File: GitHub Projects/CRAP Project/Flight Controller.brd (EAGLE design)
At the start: 40 x 75 mm, 47 parts

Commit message: Changed Module Offsets
Changed module offsets to different values so that the giant names would
go away.  I feel that in future versions this feature will be more
refined, since in V7.7 was the very first version it appeared in.  The
manual inside of the Eagle install in C:/ thankfully is updated with the
new features and explains some of the new ways to do things better than
anywhere I can find online.  Seems that nobody online has these issues,
or I suppose that they just automatically think to read the 1000 page
document every update.
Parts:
- renumbered DCDC_REGULATOR1:C1 to C101, DCDC_REGULATOR1:C10 to C110, DCDC_REGULATOR1:C11 to C111, DCDC_REGULATOR1:C2 to C102, DCDC_REGULATOR1:C3 to C103, DCDC_REGULATOR1:C4 to C104, DCDC_REGULATOR1:C5 to C105, DCDC_REGULATOR1:C6 to C106, DCDC_REGULATOR1:C7 to C107, DCDC_REGULATOR1:C8 to C108, DCDC_REGULATOR1:C9 to C109, DCDC_REGULATOR1:L1 to L101, DCDC_REGULATOR1:Q1 to Q101, DCDC_REGULATOR1:Q2 to Q102, DCDC_REGULATOR1:R1 to R101, DCDC_REGULATOR1:R2 to R102, DCDC_REGULATOR1:R3 to R103, DCDC_REGULATOR1:R4 to R104, DCDC_REGULATOR1:R5 to R105, DCDC_REGULATOR1:R6 to R106, DCDC_REGULATOR1:U$1 to U$101, M:C1 to C201, M:U1 to U201, ORDNANCE1:C1 to C301, ORDNANCE1:C2 to C302, ORDNANCE1:C3 to C303, ORDNANCE1:C4 to C304, ORDNANCE1:R1 to R301, ORDNANCE1:R2 to R302, ORDNANCE1:R3 to R303, ORDNANCE1:R4 to R304, ORDNANCE1:U1 to U301, RTD1:C1 to C401, RTD1:C2 to C402, RTD1:C3 to C403, RTD1:C4 to C404, RTD1:C5 to C405, RTD1:C6 to C406, RTD1:C7 to C407, RTD1:R2 to R402, RTD1:R4 to R404, RTD1:R5 to R405, RTD1:R6 to R406, RTD1:R7 to R407, RTD1:U$1 to U$401, RTD1:U$2 to U$402
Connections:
- net M:+3V3 renamed MS5611:+3V3
- net M:GND renamed MS5611:GND

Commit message: RTD module nearly done
1. RTD module is nearly done. Just need to figure out the connections in
and out of modules, especially for the serial data lines and power.
2. Touched up power and ordnance modules to include the correct ground
symbols.
Note: All this was done with the Eagle 7.x version files
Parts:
- removed C404, C405, C406, C407: 1u, rcl:C0603
- removed R405, R406, R407: 15k, rcl:R0603
- removed U$402: MAX4377T, maxim:UMAX8
- added J401: 4POS_SCREWTERM, CRAP Parts:4POS_0.1
- added R401, R403: 1.2 k, rcl:R0603
- C401, C402: value 1u -> 0.1 u
- C403: value 1u -> 100 n
- R402: value 15k -> 1.2 k
- R404: value 15k -> 10 M
- U$401: value MCP1501-18 -> MAX31865; device microchip:SOT23-6 -> maxim:TQFN20-5X5
- moved R402 16.5 mm to (-53.0, -187.0)
- moved C401 13.3 mm to (-51.0, -170.0)
- moved R404 11.4 mm to (-53.0, -197.0)
- moved U$401 11.0 mm to (-50.0, -162.0)
- moved C402 8.54 mm to (-51.0, -174.0)
- moved C403 5.00 mm to (-51.0, -178.0)
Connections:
- net DCDC_REGULATOR1:N$6 renamed DCDC_REGULATOR1:3V3_OUT_RTN
- removed net DCDC_REGULATOR1:N$15: C101.2, C102.2, C103.2
- removed net DCDC_REGULATOR1:N$8: U$101.P$10, U$101.P$4
- removed net ORDNANCE1:N$4: C301.2, C303.2
- removed net ORDNANCE1:N$7: R303.1
- removed net ORDNANCE1:N$9: U301.P11, U301.P8
- removed net RTD1:S1+: U$402.3
- removed net RTD1:S1–: U$402.2
- removed net RTD1:S2+: U$402.5
- removed net RTD1:S2–: U$402.6
- new net DCDC_REGULATOR1:GND: C101.2, C102.2, C103.2, C104.2, C105.2, Q101.1, R102.2, U$101.P$10, U$101.P$4
- new net ORDNANCE1:GND: C301.2, C303.2, C304.2, R303.1, U301.P11, U301.P8
- new net RTD1:N$14: U$401.18
- new net RTD1:N$5: R404.1, U$401.2
- new net RTD1:N$6: C403.1, J401.P$3, U$401.7
- net DCDC_REGULATOR1:N$2: no longer Q101.1
- net RTD1:GND: now also C401.2, C402.2, U$401.10, U$401.15, U$401.16, U$401.6, U$401.EXP; no longer U$402.4
- net RTD1:N$1: now also R401.2, R403.2, R404.2; no longer C402.1
- net RTD1:N$10: now also U$401.13; no longer R406.2, U$402.7
- net RTD1:N$11: now also J401.P$4, U$401.5; no longer C406.1, R406.1, R407.2
- net RTD1:N$12: now also U$401.12; no longer C407.1, R407.1
- net RTD1:N$13: now also U$401.11; no longer C405.2, U$402.8
- net RTD1:N$2: now also C402.1, U$401.19; no longer C401.1, U$401.6
- net RTD1:N$3: now also C401.1, U$401.20; no longer U$401.2, U$401.3
- net RTD1:N$4: now also R401.1, R402.1, R403.1, U$401.3, U$401.4; no longer U$401.5
- net RTD1:N$7: now also C403.2, J401.P$2, U$401.8; no longer R404.2, U$402.1
- net RTD1:N$8: now also J401.P$1, U$401.9; no longer C403.1, R404.1, R405.2
- net RTD1:N$9: now also U$401.14; no longer C404.1, R405.1

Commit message: Fixed the board consistency by making a new board
Do not modify the schematic unless the schematic and board are
consistant.  The easiest way to do this is to just have the board open
when you open the schematic.  This is why it asks if you want to open
both when you first open the program.

Also added a fancy logo to the Atmel chip's footprint, also found an
existing part for the Xbee900 Pro, so I added that into the schematic
and made a module for it.

Also added in modules for the memory and GPS.  That will be what I work
on next.

Outstanding things:  I think the power module is a little funky with the
ports you have on there, Cooper. Are the two return lines not a common
ground?  Why separate them?  Also I recommend changing the ports on the
module to reflect any new net name changes, as well as having a
consistent direction of the pin, so set them to "pwr" when you create
them.  This will come in handy later with design rule checks, because
it'll flag any inconsistancies.
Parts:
- added C1: 4.7u, rcl:C0603
- added C2, C502: 1u, rcl:C0603
- added C3: 100n, rcl:C0603
- added C501: 0.1u, rcl:C0603
- added D301: STPS3045C, diode:TO263AB
- added ORDNANCE1:FIRING_CIRCUIT1:R1, ORDNANCE1:FIRING_CIRCUIT1:R2, ORDNANCE1:FIRING_CIRCUIT1:R3, ORDNANCE1:FIRING_CIRCUIT1:R4: 10 k, rcl:R0603
- added ORDNANCE1:FIRING_CIRCUIT1:U$1: PMF170XP, transistor-power:SOT323
- added ORDNANCE1:FIRING_CIRCUIT1:U$2: DMG4800LSD, transistor-power:SO-08
- added U$1: 2POS_SCREWTERM, CRAP Parts:2POS_0.1
- added U1: (no value), atmel:SQFP-S-10X10-64
- added XB501: XBEE-PRO, maxstream:XBEE-PRO
- JP1: device pinhead:2X03 -> atmel:2X05
- moved R404 308.8 mm to (-24.1, 110.5)
- moved R403 304.5 mm to (-17.8, 110.5)
- moved R402 287.9 mm to (-71.1, 100.3)
- moved R401 282.6 mm to (-64.8, 100.3)
- moved C403 278.4 mm to (-45.7, 100.3)
- moved C402 274.4 mm to (-58.4, 100.3)
- moved C401 270.3 mm to (-52.1, 100.3)
- moved U$401 266.5 mm to (-20.3, 102.9)
- moved J401 262.6 mm to (-35.6, 101.6)
- moved C304 218.7 mm to (-24.1, 66.0)
- moved R304 194.8 mm to (-71.1, 45.7)
- moved C303 194.4 mm to (-17.8, 66.0)
- moved C111 192.9 mm to (-41.9, 88.9)
- moved R303 189.0 mm to (-64.8, 45.7)
- moved C110 186.0 mm to (-35.6, 88.9)
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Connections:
- removed net DCDC_REGULATOR1:3V3_OUT: C106.1, C107.1, C108.1, C109.1, C110.1, C111.1, R103.2, R105.2, U$101.P$7, U$101.P$8
- removed net MS5611:+3V3: C201.1, U201.1
- removed net MS5611:GND: C201.2, U201.2, U201.3
- removed net X_PDI_DATA: JP1.6
- removed net X_RESET_PDI_CLK: JP1.2
- new net N$1: JP1.2, U1.54
- new net N$2: JP1.4, U1.55
- new net N$3: JP1.6, U1.50
- new net N$4: JP1.8, U1.62
- new net N$5: JP1.10, U1.2
- new net N$9: U$1.P$2
- new net ORDNANCE1:FIRING_CIRCUIT1:GND: ORDNANCE1:FIRING_CIRCUIT1:R2.1, ORDNANCE1:FIRING_CIRCUIT1:R3.1, ORDNANCE1:FIRING_CIRCUIT1:U$2.3
- new net ORDNANCE1:FIRING_CIRCUIT1:N$1: ORDNANCE1:FIRING_CIRCUIT1:U$2.1, ORDNANCE1:FIRING_CIRCUIT1:U$2.5, ORDNANCE1:FIRING_CIRCUIT1:U$2.6
- new net ORDNANCE1:FIRING_CIRCUIT1:N$2: ORDNANCE1:FIRING_CIRCUIT1:U$2.7, ORDNANCE1:FIRING_CIRCUIT1:U$2.8
- new net ORDNANCE1:FIRING_CIRCUIT1:N$3: ORDNANCE1:FIRING_CIRCUIT1:R1.1
- new net ORDNANCE1:FIRING_CIRCUIT1:N$4: ORDNANCE1:FIRING_CIRCUIT1:R3.2, ORDNANCE1:FIRING_CIRCUIT1:U$2.2
- new net ORDNANCE1:FIRING_CIRCUIT1:N$5: ORDNANCE1:FIRING_CIRCUIT1:R2.2, ORDNANCE1:FIRING_CIRCUIT1:U$2.4
- new net ORDNANCE1:FIRING_CIRCUIT1:N$6: ORDNANCE1:FIRING_CIRCUIT1:R1.2, ORDNANCE1:FIRING_CIRCUIT1:U$1.1
- new net ORDNANCE1:FIRING_CIRCUIT1:N$7: ORDNANCE1:FIRING_CIRCUIT1:R4.1, ORDNANCE1:FIRING_CIRCUIT1:U$1.2
- new net ORDNANCE1:FIRING_CIRCUIT1:N$8: ORDNANCE1:FIRING_CIRCUIT1:R4.2, ORDNANCE1:FIRING_CIRCUIT1:U$1.3
- new net ORDNANCE1:N$4: D301.1, D301.2
- new net ORDNANCE1:N$7: D301.K
- new net VCC_IN: U$1.P$1
- new net VDDOUT: C2.2, C3.2, U1.30, U1.45, U1.9
- new net XBEE900-1:XBEE_UART_IN: XB501.3
- new net XBEE900-1:XBEE_UART_OUT: XB501.2
- net +3V3: now also C1.1, C106.1, C107.1, C108.1, C109.1, C110.1, C111.1, C201.1, C501.1, C502.1, JP1.1, R103.2, R105.2, U$101.P$7, U$101.P$8, U1.1, U1.27, U1.31, U1.32, U1.64, U201.1, XB501.1; no longer JP1.5
- net DCDC_REGULATOR1:GND: now also R104.1
- net GND: now also C1.2, C2.1, C201.2, C3.1, C501.2, C502.2, JP1.3, JP1.5, JP1.9, U1.13, U1.29, U1.53, U201.2, U201.3, XB501.10; no longer JP1.1
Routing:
- net MS5611_MISO: track 14.7 -> 0.00 mm, vias 2 -> 0
- net X_PDI_DATA: track 11.8 -> 0.00 mm
- net MS5611_SCLK: track 6.11 -> 0.00 mm
- net MS5611:+3V3: track 5.43 -> 0.00 mm
- net MS5611_MOSI: track 5.25 -> 0.00 mm
- net MS5611_CS: track 4.34 -> 0.00 mm
- removed copper zone on layer 1, net N$1
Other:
- board text removed: "PROG"

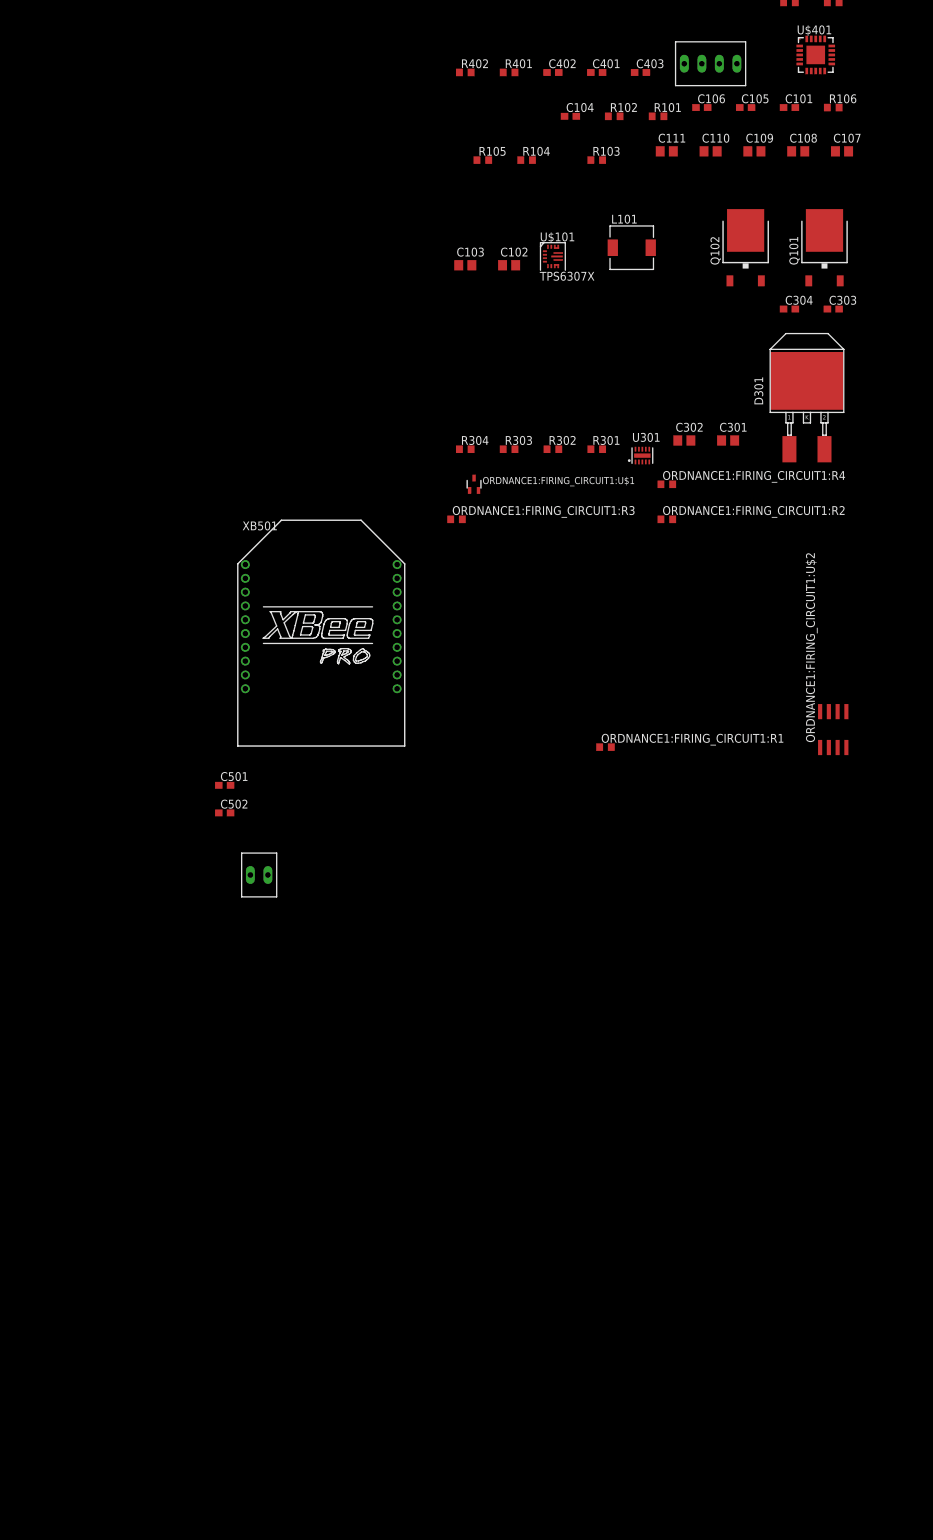
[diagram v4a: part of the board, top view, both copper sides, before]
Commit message: Module updates
1. Fixed or added ports to the following modules: DC-DC Converter, RTD,
Ordnance, and Firing Chains
2. Fixed power pins within those modules
3. Minor updates to the DC-DC Converter regarding the connections to the
TPS63070
4. Moved the RTD's screw terminal block to the top level sheet
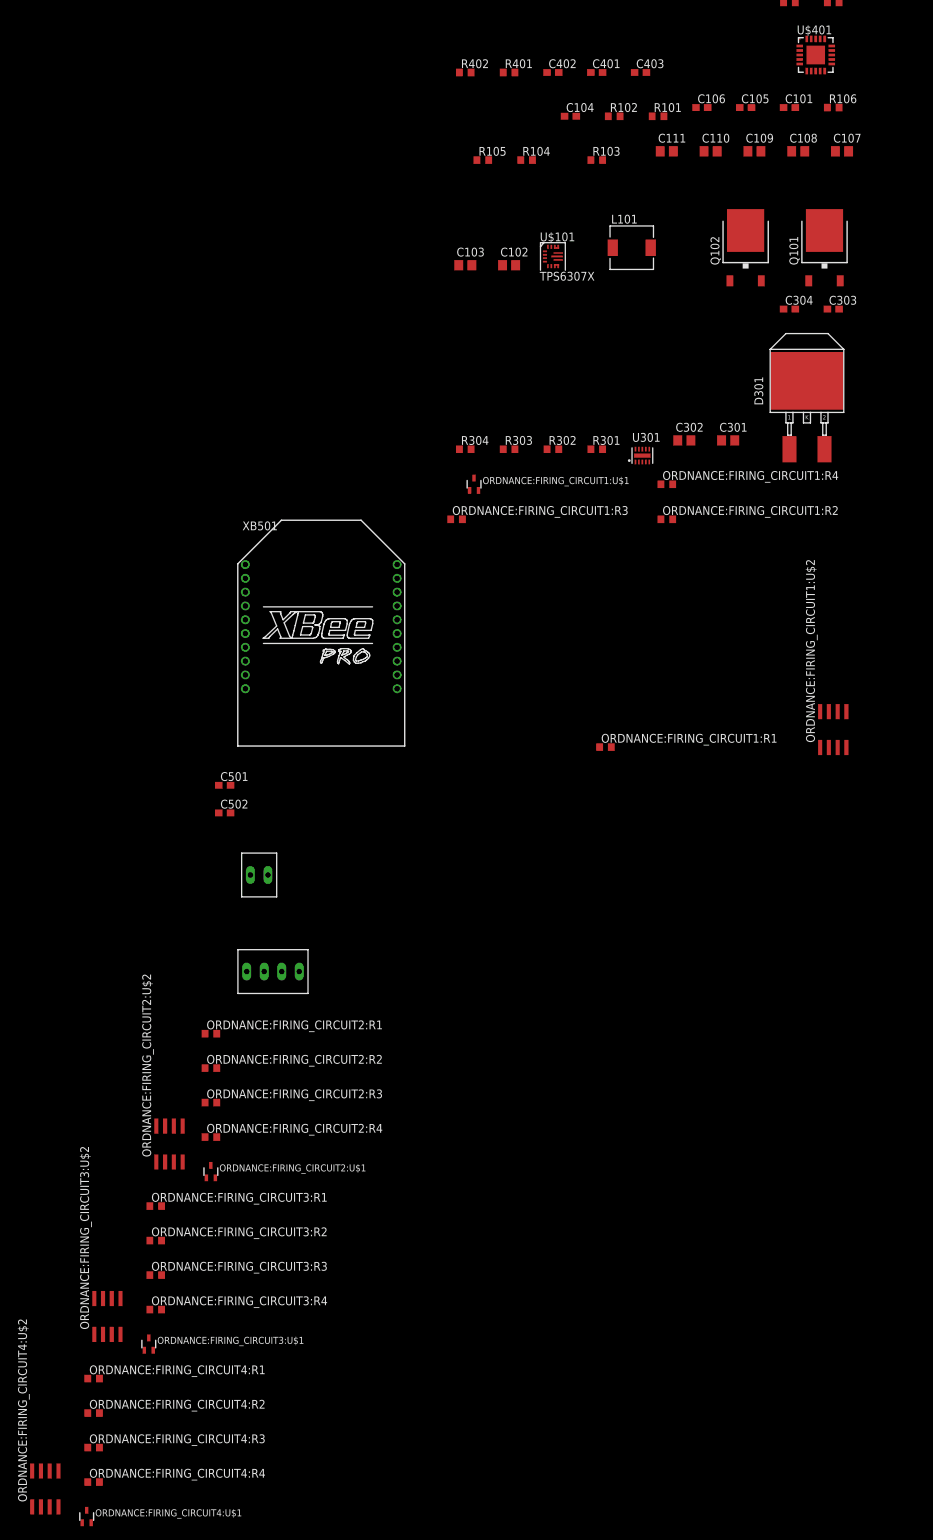
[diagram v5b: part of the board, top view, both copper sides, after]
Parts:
- removed J401: 4POS_SCREWTERM, CRAP Parts:4POS_0.1
- added J2: 4POS_SCREWTERM, CRAP Parts:4POS_0.1
- added ORDNANCE:FIRING_CIRCUIT2:R1, ORDNANCE:FIRING_CIRCUIT2:R2, ORDNANCE:FIRING_CIRCUIT2:R3, ORDNANCE:FIRING_CIRCUIT2:R4, ORDNANCE:FIRING_CIRCUIT3:R1, ORDNANCE:FIRING_CIRCUIT3:R2, ORDNANCE:FIRING_CIRCUIT3:R3, ORDNANCE:FIRING_CIRCUIT3:R4, ORDNANCE:FIRING_CIRCUIT4:R1, ORDNANCE:FIRING_CIRCUIT4:R2, ORDNANCE:FIRING_CIRCUIT4:R3, ORDNANCE:FIRING_CIRCUIT4:R4: 10 k, rcl:R0603
- added ORDNANCE:FIRING_CIRCUIT2:U$1, ORDNANCE:FIRING_CIRCUIT3:U$1, ORDNANCE:FIRING_CIRCUIT4:U$1: PMF170XP, transistor-power:SOT323
- added ORDNANCE:FIRING_CIRCUIT2:U$2, ORDNANCE:FIRING_CIRCUIT3:U$2, ORDNANCE:FIRING_CIRCUIT4:U$2: DMG4800LSD, transistor-power:SO-08
- renumbered ORDNANCE1:FIRING_CIRCUIT1:R1 to ORDNANCE:FIRING_CIRCUIT1:R1, ORDNANCE1:FIRING_CIRCUIT1:R2 to ORDNANCE:FIRING_CIRCUIT1:R2, ORDNANCE1:FIRING_CIRCUIT1:R3 to ORDNANCE:FIRING_CIRCUIT1:R3, ORDNANCE1:FIRING_CIRCUIT1:R4 to ORDNANCE:FIRING_CIRCUIT1:R4, ORDNANCE1:FIRING_CIRCUIT1:U$1 to ORDNANCE:FIRING_CIRCUIT1:U$1, ORDNANCE1:FIRING_CIRCUIT1:U$2 to ORDNANCE:FIRING_CIRCUIT1:U$2, U$1 to J1
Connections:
- net DCDC_REGULATOR1:N$1 renamed DCDC_REGULATOR:N$1
- net DCDC_REGULATOR1:N$10 renamed DCDC_REGULATOR:N$10
- net DCDC_REGULATOR1:N$11 renamed DCDC_REGULATOR:N$11
- net DCDC_REGULATOR1:N$2 renamed DCDC_REGULATOR:N$2
- net DCDC_REGULATOR1:N$3 renamed DCDC_REGULATOR:N$3
- net DCDC_REGULATOR1:N$4 renamed DCDC_REGULATOR:N$4
- net DCDC_REGULATOR1:N$5 renamed DCDC_REGULATOR:N$5
- net DCDC_REGULATOR1:N$7 renamed DCDC_REGULATOR:N$7
- net DCDC_REGULATOR1:N$9 renamed DCDC_REGULATOR:N$9
- net ORDNANCE1:!SHDN renamed ORDNANCE:!SHDN
- net ORDNANCE1:FIRING_CIRCUIT1:GND renamed ORDNANCE:FIRING_CIRCUIT1:GND
- net ORDNANCE1:FIRING_CIRCUIT1:N$1 renamed ORDNANCE:FIRING_CIRCUIT1:N$1
- net ORDNANCE1:FIRING_CIRCUIT1:N$2 renamed ORDNANCE:FIRING_CIRCUIT1:N$2
- net ORDNANCE1:FIRING_CIRCUIT1:N$3 renamed ORDNANCE:FIRING_CIRCUIT1:N$3
- net ORDNANCE1:FIRING_CIRCUIT1:N$4 renamed ORDNANCE:FIRING_CIRCUIT1:FIRE1
- net ORDNANCE1:FIRING_CIRCUIT1:N$5 renamed ORDNANCE:FIRING_CIRCUIT1:FIRE2
- net ORDNANCE1:FIRING_CIRCUIT1:N$6 renamed ORDNANCE:FIRING_CIRCUIT1:N$6
- net ORDNANCE1:FIRING_CIRCUIT1:N$7 renamed ORDNANCE:FIRING_CIRCUIT1:N$7
- net ORDNANCE1:FIRING_CIRCUIT1:N$8 renamed ORDNANCE:FIRING_CIRCUIT1:+3V3
- net ORDNANCE1:N$1 renamed ORDNANCE:N$1
- net ORDNANCE1:N$10 renamed ORDNANCE:N$10
- net ORDNANCE1:N$2 renamed ORDNANCE:N$2
- net ORDNANCE1:N$4 renamed ORDNANCE:N$4
- net ORDNANCE1:N$5 renamed ORDNANCE:N$5
- net ORDNANCE1:N$6 renamed ORDNANCE:N$6
- net ORDNANCE1:N$7 renamed ORDNANCE:N$7
- net ORDNANCE1:N$8 renamed ORDNANCE:N$8
- net ORDNANCE1:ORD_PWR renamed ORDNANCE:ORD_PWR
- net RTD1:N$1 renamed RTD:N$1
- net RTD1:N$10 renamed RTD:!CS
- net RTD1:N$12 renamed RTD:SCLK
- net RTD1:N$13 renamed RTD:SDI
- net RTD1:N$14 renamed RTD:!DRDY
- net RTD1:N$4 renamed RTD:N$4
- net RTD1:N$5 renamed RTD:N$5
- net RTD1:N$9 renamed RTD:SDO
- removed net DCDC_REGULATOR1:3V3_OUT_RTN: C106.2, C107.2, C108.2, C109.2, C110.2, C111.2
- removed net DCDC_REGULATOR1:GND: C101.2, C102.2, C103.2, C104.2, C105.2, Q101.1, R102.2, R104.1, U$101.P$10, U$101.P$4
- removed net DCDC_REGULATOR1:PWR_IN: Q101.2
- removed net ORDNANCE1:GND: C301.2, C303.2, C304.2, R303.1, U301.P11, U301.P8
- removed net ORDNANCE1:N$3: C301.1, C303.1, R301.2, U301.P9
- removed net RTD1:GND: C401.2, C402.2, U$401.10, U$401.15, U$401.16, U$401.6, U$401.EXP
- removed net RTD1:N$11: J401.P$4, U$401.5
- removed net RTD1:N$2: C402.1, U$401.19
- removed net RTD1:N$3: C401.1, U$401.20
- removed net RTD1:N$6: C403.1, J401.P$3, U$401.7
- removed net RTD1:N$7: C403.2, J401.P$2, U$401.8
- removed net RTD1:N$8: J401.P$1, U$401.9
- new net DCDC_REGULATOR:GND: C101.2, C102.2, C103.2, C104.2, C105.2, C106.2, C107.2, C108.2, C109.2, C110.2, C111.2, Q101.1, R104.1, U$101.P$10, U$101.P$15, U$101.P$4, U$101.P$6
- new net DCDC_REGULATOR:N$6: R102.2
- new net N$6: J2.P$1, U$401.5
- new net N$7: C403.1, J2.P$2, U$401.7
- new net N$8: C403.2, J2.P$3, U$401.8
- new net ORDNANCE:FIRING_CIRCUIT2:+3V3: ORDNANCE:FIRING_CIRCUIT2:R4.2, ORDNANCE:FIRING_CIRCUIT2:U$1.3
- new net ORDNANCE:FIRING_CIRCUIT2:FIRE1: ORDNANCE:FIRING_CIRCUIT2:R3.2, ORDNANCE:FIRING_CIRCUIT2:U$2.2
- new net ORDNANCE:FIRING_CIRCUIT2:FIRE2: ORDNANCE:FIRING_CIRCUIT2:R2.2, ORDNANCE:FIRING_CIRCUIT2:U$2.4
- new net ORDNANCE:FIRING_CIRCUIT2:GND: ORDNANCE:FIRING_CIRCUIT2:R2.1, ORDNANCE:FIRING_CIRCUIT2:R3.1, ORDNANCE:FIRING_CIRCUIT2:U$2.3
- new net ORDNANCE:FIRING_CIRCUIT2:N$1: ORDNANCE:FIRING_CIRCUIT2:U$2.1, ORDNANCE:FIRING_CIRCUIT2:U$2.5, ORDNANCE:FIRING_CIRCUIT2:U$2.6
- new net ORDNANCE:FIRING_CIRCUIT2:N$2: ORDNANCE:FIRING_CIRCUIT2:U$2.7, ORDNANCE:FIRING_CIRCUIT2:U$2.8
- new net ORDNANCE:FIRING_CIRCUIT2:N$3: ORDNANCE:FIRING_CIRCUIT2:R1.1
- new net ORDNANCE:FIRING_CIRCUIT2:N$6: ORDNANCE:FIRING_CIRCUIT2:R1.2, ORDNANCE:FIRING_CIRCUIT2:U$1.1
- new net ORDNANCE:FIRING_CIRCUIT2:N$7: ORDNANCE:FIRING_CIRCUIT2:R4.1, ORDNANCE:FIRING_CIRCUIT2:U$1.2
- new net ORDNANCE:FIRING_CIRCUIT3:+3V3: ORDNANCE:FIRING_CIRCUIT3:R4.2, ORDNANCE:FIRING_CIRCUIT3:U$1.3
- new net ORDNANCE:FIRING_CIRCUIT3:FIRE1: ORDNANCE:FIRING_CIRCUIT3:R3.2, ORDNANCE:FIRING_CIRCUIT3:U$2.2
- new net ORDNANCE:FIRING_CIRCUIT3:FIRE2: ORDNANCE:FIRING_CIRCUIT3:R2.2, ORDNANCE:FIRING_CIRCUIT3:U$2.4
- new net ORDNANCE:FIRING_CIRCUIT3:GND: ORDNANCE:FIRING_CIRCUIT3:R2.1, ORDNANCE:FIRING_CIRCUIT3:R3.1, ORDNANCE:FIRING_CIRCUIT3:U$2.3
- new net ORDNANCE:FIRING_CIRCUIT3:N$1: ORDNANCE:FIRING_CIRCUIT3:U$2.1, ORDNANCE:FIRING_CIRCUIT3:U$2.5, ORDNANCE:FIRING_CIRCUIT3:U$2.6
- new net ORDNANCE:FIRING_CIRCUIT3:N$2: ORDNANCE:FIRING_CIRCUIT3:U$2.7, ORDNANCE:FIRING_CIRCUIT3:U$2.8
- new net ORDNANCE:FIRING_CIRCUIT3:N$3: ORDNANCE:FIRING_CIRCUIT3:R1.1
- new net ORDNANCE:FIRING_CIRCUIT3:N$6: ORDNANCE:FIRING_CIRCUIT3:R1.2, ORDNANCE:FIRING_CIRCUIT3:U$1.1
- new net ORDNANCE:FIRING_CIRCUIT3:N$7: ORDNANCE:FIRING_CIRCUIT3:R4.1, ORDNANCE:FIRING_CIRCUIT3:U$1.2
- new net ORDNANCE:FIRING_CIRCUIT4:+3V3: ORDNANCE:FIRING_CIRCUIT4:R4.2, ORDNANCE:FIRING_CIRCUIT4:U$1.3
- new net ORDNANCE:FIRING_CIRCUIT4:FIRE1: ORDNANCE:FIRING_CIRCUIT4:R3.2, ORDNANCE:FIRING_CIRCUIT4:U$2.2
- new net ORDNANCE:FIRING_CIRCUIT4:FIRE2: ORDNANCE:FIRING_CIRCUIT4:R2.2, ORDNANCE:FIRING_CIRCUIT4:U$2.4
- new net ORDNANCE:FIRING_CIRCUIT4:GND: ORDNANCE:FIRING_CIRCUIT4:R2.1, ORDNANCE:FIRING_CIRCUIT4:R3.1, ORDNANCE:FIRING_CIRCUIT4:U$2.3
- new net ORDNANCE:FIRING_CIRCUIT4:N$1: ORDNANCE:FIRING_CIRCUIT4:U$2.1, ORDNANCE:FIRING_CIRCUIT4:U$2.5, ORDNANCE:FIRING_CIRCUIT4:U$2.6
- new net ORDNANCE:FIRING_CIRCUIT4:N$2: ORDNANCE:FIRING_CIRCUIT4:U$2.7, ORDNANCE:FIRING_CIRCUIT4:U$2.8
- new net ORDNANCE:FIRING_CIRCUIT4:N$3: ORDNANCE:FIRING_CIRCUIT4:R1.1
- new net ORDNANCE:FIRING_CIRCUIT4:N$6: ORDNANCE:FIRING_CIRCUIT4:R1.2, ORDNANCE:FIRING_CIRCUIT4:U$1.1
- new net ORDNANCE:FIRING_CIRCUIT4:N$7: ORDNANCE:FIRING_CIRCUIT4:R4.1, ORDNANCE:FIRING_CIRCUIT4:U$1.2
- net +3V3: now also C301.1, C303.1, C401.1, C402.1, R301.2, U$401.19, U$401.20, U301.P9
- net GND: now also C301.2, C303.2, C304.2, C401.2, C402.2, J1.P$2, R303.1, U$401.10, U$401.15, U$401.16, U$401.6, U$401.EXP, U301.P11, U301.P8
- net N$9: now also J2.P$4, U$401.9; no longer J1.P$2
- net VCC_IN: now also Q101.2
